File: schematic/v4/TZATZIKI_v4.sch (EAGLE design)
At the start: 7 parts, among them J1 2X20-CHIP-HEADERS2X20CHIP_OFF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

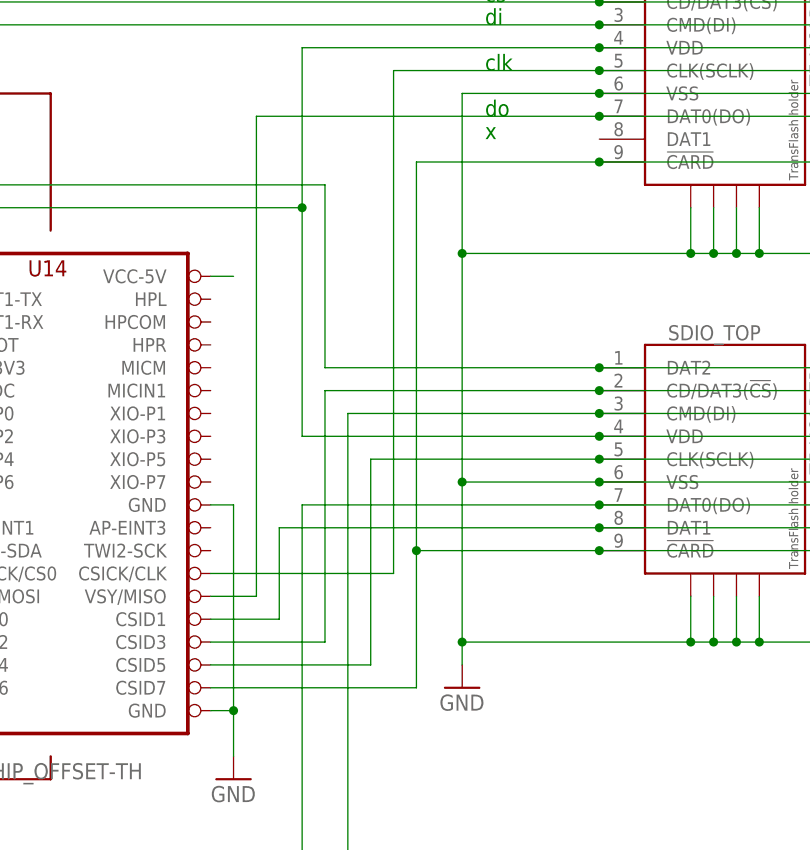
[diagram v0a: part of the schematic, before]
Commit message: moved to eint3 for Card detection
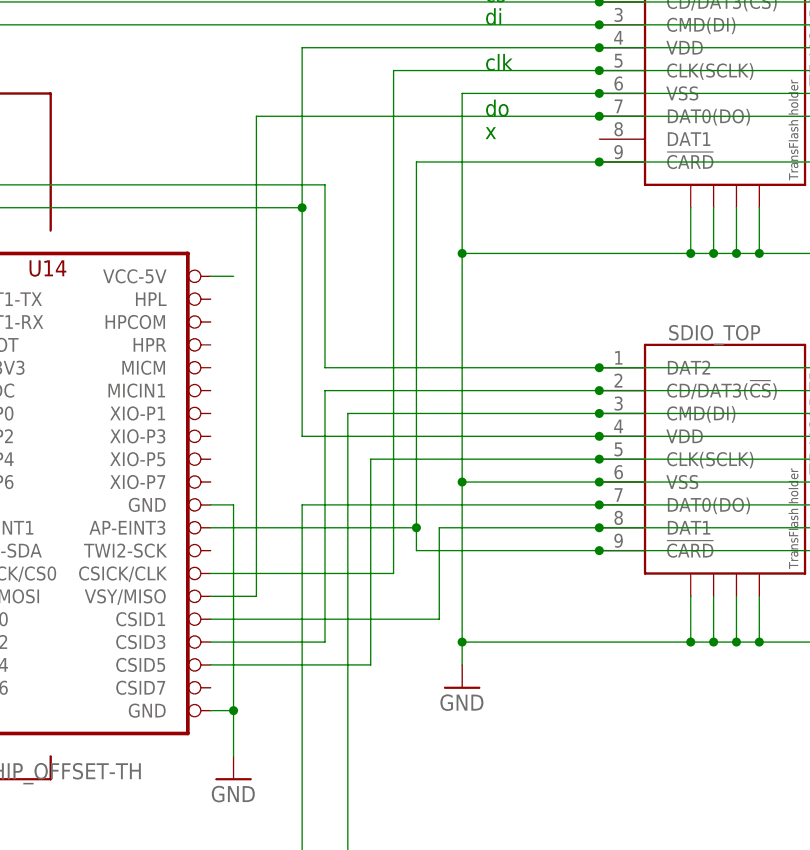
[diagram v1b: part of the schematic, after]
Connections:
- net N$16: now also J1.AP-EINT3; no longer J1.CSID7
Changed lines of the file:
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@@
 <segment>
 <pinref part="J1" gate="G$1" pin="CSID1"/>
-<wire x1="109.22" y1="25.4" x2="116.84" y2="25.4" width="0.1524" layer="91"/>
-<wire x1="116.84" y1="25.4" x2="116.84" y2="35.56" width="0.1524" layer="91"/>
+<wire x1="109.22" y1="25.4" x2="134.62" y2="25.4" width="0.1524" layer="91"/>
+<wire x1="134.62" y1="25.4" x2="134.62" y2="35.56" width="0.1524" layer="91"/>
 <wire x1="185.42" y1="35.56" x2="152.4" y2="35.56" width="0.1524" layer="91"/>
 <pinref part="SDIO_BOT" gate="G$1" pin="DAT1"/>
 <pinref part="SDIO_TOP" gate="G$1" pin="DAT1"/>
-<wire x1="152.4" y1="35.56" x2="116.84" y2="35.56" width="0.1524" layer="91"/>
+<wire x1="152.4" y1="35.56" x2="134.62" y2="35.56" width="0.1524" layer="91"/>
 <junction x="152.4" y="35.56"/>
 </segment>
@@
 <wire x1="185.42" y1="76.2" x2="152.4" y2="76.2" width="0.1524" layer="91"/>
 <pinref part="SDIO_TOP" gate="G$1" pin="!CARD"/>
-<pinref part="J1" gate="G$1" pin="CSID7"/>
-<wire x1="109.22" y1="17.78" x2="132.08" y2="17.78" width="0.1524" layer="91"/>
-<wire x1="132.08" y1="17.78" x2="132.08" y2="33.02" width="0.1524" layer="91"/>
 <wire x1="132.08" y1="33.02" x2="152.4" y2="33.02" width="0.1524" layer="91"/>
 <pinref part="SDIO_BOT" gate="G$1" pin="!CARD"/>
@@
 <junction x="152.4" y="33.02"/>
 <wire x1="152.4" y1="76.2" x2="132.08" y2="76.2" width="0.1524" layer="91"/>
-<wire x1="132.08" y1="76.2" x2="132.08" y2="33.02" width="0.1524" layer="91"/>
-<junction x="132.08" y="33.02"/>
+<wire x1="132.08" y1="76.2" x2="132.08" y2="35.56" width="0.1524" layer="91"/>
 <junction x="152.4" y="76.2"/>
+<pinref part="J1" gate="G$1" pin="AP-EINT3"/>
+<wire x1="132.08" y1="35.56" x2="132.08" y2="33.02" width="0.1524" layer="91"/>
+<wire x1="109.22" y1="35.56" x2="132.08" y2="35.56" width="0.1524" layer="91"/>
+<junction x="132.08" y="35.56"/>
 </segment>
 </net>

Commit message: added gerber
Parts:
- removed SPI_BOT, SPI_TOP: TF-HOLDER, JKW_CHIP:TF-HOLDER
- added R10: 2.2k, rcl:R-EU_R0805
- added U2: DS2431P, JKW_CHIP:DS2431P
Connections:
- removed net N$11: J1.CSIPCK/CS0, SPI_BOT.CD/DAT3(!CS!), SPI_TOP.CD/DAT3(!CS!)
- removed net N$12: J1.HSY/MOSI, SPI_BOT.CMD(DI), SPI_TOP.CMD(DI)
- removed net N$13: J1.VSY/MISO, SPI_BOT.DAT0(DO), SPI_TOP.DAT0(DO)
- removed net N$14: J1.CSICK/CLK, SPI_BOT.CLK(SCLK), SPI_TOP.CLK(SCLK)
- new net LD2: J1.LCD-D2, R10.1, U2.IO
- new net N$1: J1.VCC3V3@2, R10.2
- net GND: now also U2.GND; no longer SPI_BOT.S1, SPI_BOT.S2, SPI_BOT.S3, SPI_BOT.S4, SPI_BOT.VSS, SPI_TOP.S1, SPI_TOP.S2, SPI_TOP.S3, SPI_TOP.S4, SPI_TOP.VSS
- net N$10: no longer SPI_BOT.VDD, SPI_TOP.VDD
- net N$16: no longer SPI_BOT.!CARD, SPI_TOP.!CARD
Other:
- note removed: "clk"
- note removed: "cs"
- note removed: "di"
- note removed: "do"
- note removed: "x"
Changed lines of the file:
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@@
 <part name="SDIO_BOT" library="JKW_CHIP" deviceset="TF-HOLDER" device=""/>
 <part name="SDIO_TOP" library="JKW_CHIP" deviceset="TF-HOLDER" device=""/>
-<part name="SPI_TOP" library="JKW_CHIP" deviceset="TF-HOLDER" device=""/>
-<part name="SPI_BOT" library="JKW_CHIP" deviceset="TF-HOLDER" device=""/>
+<part name="GND14" library="supply1" deviceset="GND" device=""/>
+<part name="R10" library="rcl" deviceset="R-EU_" device="R0805" value="2.2k"/>
+<part name="U2" library="JKW_CHIP" deviceset="DS2431" device="P"/>
 </parts>
 <sheets>
 <sheet>
 <plain>
-<text x="139.7" y="93.98" size="1.778" layer="91">cs</text>
-<text x="139.7" y="91.44" size="1.778" layer="91">di</text>
-<text x="139.7" y="86.36" size="1.778" layer="91">clk</text>
-<text x="139.7" y="81.28" size="1.778" layer="91">do</text>
-<text x="139.7" y="78.74" size="1.778" layer="91">x</text>
-<text x="139.7" y="96.52" size="1.778" layer="91">x</text>
 </plain>
 <instances>
@@
 <instance part="SDIO_BOT" gate="G$1" x="198.12" y="43.18"/>
 <instance part="SDIO_TOP" gate="G$1" x="165.1" y="43.18"/>
-<instance part="SPI_TOP" gate="G$1" x="165.1" y="86.36"/>
-<instance part="SPI_BOT" gate="G$1" x="198.12" y="86.36"/>
+<instance part="GND14" gate="1" x="-35.56" y="12.7" rot="MR0"/>
+<instance part="R10" gate="G$1" x="-7.62" y="43.18" rot="MR90"/>
+<instance part="U2" gate="G$1" x="-33.02" y="33.02"/>
 </instances>
 <busses>
@@
 <wire x1="137.16" y1="40.64" x2="137.16" y2="22.86" width="0.1524" layer="91"/>
 <junction x="137.16" y="22.86"/>
-<wire x1="137.16" y1="83.82" x2="137.16" y2="66.04" width="0.1524" layer="91"/>
-<wire x1="137.16" y1="40.64" x2="137.16" y2="66.04" width="0.1524" layer="91"/>
-<junction x="137.16" y="66.04"/>
-<junction x="137.16" y="40.64"/>
 <wire x1="203.2" y1="22.86" x2="200.66" y2="22.86" width="0.1524" layer="91"/>
 <wire x1="200.66" y1="22.86" x2="198.12" y2="22.86" width="0.1524" layer="91"/>
@@
 <wire x1="185.42" y1="40.64" x2="152.4" y2="40.64" width="0.1524" layer="91"/>
 <wire x1="152.4" y1="40.64" x2="137.16" y2="40.64" width="0.1524" layer="91"/>
-<pinref part="SPI_BOT" gate="G$1" pin="VSS"/>
-<wire x1="137.16" y1="83.82" x2="152.4" y2="83.82" width="0.1524" layer="91"/>
-<pinref part="SPI_TOP" gate="G$1" pin="S1"/>
-<wire x1="152.4" y1="83.82" x2="185.42" y2="83.82" width="0.1524" layer="91"/>
-<wire x1="137.16" y1="66.04" x2="162.56" y2="66.04" width="0.1524" layer="91"/>
-<wire x1="162.56" y1="66.04" x2="162.56" y2="71.12" width="0.1524" layer="91"/>
-<pinref part="SPI_BOT" gate="G$1" pin="S4"/>
-<wire x1="162.56" y1="66.04" x2="165.1" y2="66.04" width="0.1524" layer="91"/>
-<wire x1="165.1" y1="66.04" x2="167.64" y2="66.04" width="0.1524" layer="91"/>
-<wire x1="167.64" y1="66.04" x2="170.18" y2="66.04" width="0.1524" layer="91"/>
-<wire x1="170.18" y1="66.04" x2="195.58" y2="66.04" width="0.1524" layer="91"/>
-<wire x1="195.58" y1="66.04" x2="198.12" y2="66.04" width="0.1524" layer="91"/>
-<wire x1="198.12" y1="66.04" x2="200.66" y2="66.04" width="0.1524" layer="91"/>
-<wire x1="200.66" y1="66.04" x2="203.2" y2="66.04" width="0.1524" layer="91"/>
-<wire x1="203.2" y1="66.04" x2="203.2" y2="71.12" width="0.1524" layer="91"/>
-<pinref part="SPI_BOT" gate="G$1" pin="S3"/>
-<wire x1="200.66" y1="71.12" x2="200.66" y2="66.04" width="0.1524" layer="91"/>
-<pinref part="SPI_BOT" gate="G$1" pin="S2"/>
-<wire x1="198.12" y1="71.12" x2="198.12" y2="66.04" width="0.1524" layer="91"/>
-<pinref part="SPI_BOT" gate="G$1" pin="S1"/>
-<wire x1="195.58" y1="71.12" x2="195.58" y2="66.04" width="0.1524" layer="91"/>
-<pinref part="SPI_TOP" gate="G$1" pin="S4"/>
-<wire x1="170.18" y1="71.12" x2="170.18" y2="66.04" width="0.1524" layer="91"/>
-<pinref part="SPI_TOP" gate="G$1" pin="S3"/>
-<wire x1="167.64" y1="71.12" x2="167.64" y2="66.04" width="0.1524" layer="91"/>
-<pinref part="SPI_TOP" gate="G$1" pin="S2"/>
-<wire x1="165.1" y1="71.12" x2="165.1" y2="66.04" width="0.1524" layer="91"/>
-<junction x="162.56" y="66.04"/>
-<junction x="165.1" y="66.04"/>
-<junction x="167.64" y="66.04"/>
-<junction x="170.18" y="66.04"/>
-<junction x="195.58" y="66.04"/>
-<junction x="198.12" y="66.04"/>
-<junction x="200.66" y="66.04"/>
-<pinref part="SPI_TOP" gate="G$1" pin="VSS"/>
-<junction x="152.4" y="83.82"/>
 <pinref part="SDIO_BOT" gate="G$1" pin="VSS"/>
 <pinref part="SDIO_TOP" gate="G$1" pin="VSS"/>
@@
 <wire x1="-12.7" y1="76.2" x2="-12.7" y2="73.66" width="0.1524" layer="91"/>
 </segment>
+<segment>
+<pinref part="GND14" gate="1" pin="GND"/>
+<wire x1="-35.56" y1="20.32" x2="-35.56" y2="15.24" width="0.1524" layer="91"/>
+<pinref part="U2" gate="G$1" pin="GND"/>
+</segment>
 </net>
 <net name="N$2" class="0">
@@
 <wire x1="71.12" y1="71.12" x2="119.38" y2="71.12" width="0.1524" layer="91"/>
 <wire x1="119.38" y1="71.12" x2="119.38" y2="45.72" width="0.1524" layer="91"/>
-<wire x1="119.38" y1="71.12" x2="119.38" y2="88.9" width="0.1524" layer="91"/>
-<junction x="119.38" y="71.12"/>
 <wire x1="185.42" y1="45.72" x2="152.4" y2="45.72" width="0.1524" layer="91"/>
-<pinref part="SPI_BOT" gate="G$1" pin="VDD"/>
 <wire x1="152.4" y1="45.72" x2="119.38" y2="45.72" width="0.1524" layer="91"/>
-<wire x1="119.38" y1="88.9" x2="152.4" y2="88.9" width="0.1524" layer="91"/>
-<pinref part="SPI_TOP" gate="G$1" pin="VDD"/>
-<wire x1="152.4" y1="88.9" x2="185.42" y2="88.9" width="0.1524" layer="91"/>
-<junction x="152.4" y="88.9"/>
 <pinref part="SDIO_BOT" gate="G$1" pin="VDD"/>
 <pinref part="SDIO_TOP" gate="G$1" pin="VDD"/>
@@
 </segment>
 </net>
-<net name="N$11" class="0">
-<segment>
-<wire x1="152.4" y1="93.98" x2="66.04" y2="93.98" width="0.1524" layer="91"/>
-<wire x1="66.04" y1="93.98" x2="66.04" y2="30.48" width="0.1524" layer="91"/>
-<pinref part="J1" gate="G$1" pin="CSIPCK/CS0"/>
-<wire x1="66.04" y1="30.48" x2="76.2" y2="30.48" width="0.1524" layer="91"/>
-<pinref part="SPI_TOP" gate="G$1" pin="CD/DAT3(!CS!)"/>
-<pinref part="SPI_BOT" gate="G$1" pin="CD/DAT3(!CS!)"/>
-<wire x1="152.4" y1="93.98" x2="185.42" y2="93.98" width="0.1524" layer="91"/>
-<junction x="152.4" y="93.98"/>
-</segment>
-</net>
-<net name="N$12" class="0">
-<segment>
-<wire x1="63.5" y1="91.44" x2="63.5" y2="27.94" width="0.1524" layer="91"/>
-<pinref part="J1" gate="G$1" pin="HSY/MOSI"/>
-<wire x1="63.5" y1="27.94" x2="76.2" y2="27.94" width="0.1524" layer="91"/>
-<pinref part="SPI_BOT" gate="G$1" pin="CMD(DI)"/>
-<wire x1="63.5" y1="91.44" x2="152.4" y2="91.44" width="0.1524" layer="91"/>
-<pinref part="SPI_TOP" gate="G$1" pin="CMD(DI)"/>
-<wire x1="152.4" y1="91.44" x2="185.42" y2="91.44" width="0.1524" layer="91"/>
-<junction x="152.4" y="91.44"/>
-</segment>
-</net>
-<net name="N$13" class="0">
-<segment>
-<pinref part="J1" gate="G$1" pin="VSY/MISO"/>
-<wire x1="109.22" y1="27.94" x2="114.3" y2="27.94" width="0.1524" layer="91"/>
-<wire x1="114.3" y1="27.94" x2="114.3" y2="81.28" width="0.1524" layer="91"/>
-<pinref part="SPI_BOT" gate="G$1" pin="DAT0(DO)"/>
-<wire x1="114.3" y1="81.28" x2="152.4" y2="81.28" width="0.1524" layer="91"/>
-<pinref part="SPI_TOP" gate="G$1" pin="DAT0(DO)"/>
-<wire x1="152.4" y1="81.28" x2="185.42" y2="81.28" width="0.1524" layer="91"/>
-<junction x="152.4" y="81.28"/>
-</segment>
-</net>
 <net name="N$7" class="0">
 <segment>
 <pinref part="J1" gate="G$1" pin="VCC-5V@2"/>
 <wire x1="109.22" y1="63.5" x2="111.76" y2="63.5" width="0.1524" layer="91"/>
-</segment>
-</net>
-<net name="N$14" class="0">
-<segment>
-<wire x1="129.54" y1="30.48" x2="129.54" y2="86.36" width="0.1524" layer="91"/>
-<pinref part="J1" gate="G$1" pin="CSICK/CLK"/>
-<wire x1="109.22" y1="30.48" x2="129.54" y2="30.48" width="0.1524" layer="91"/>
-<pinref part="SPI_BOT" gate="G$1" pin="CLK(SCLK)"/>
-<wire x1="129.54" y1="86.36" x2="152.4" y2="86.36" width="0.1524" layer="91"/>
-<pinref part="SPI_TOP" gate="G$1" pin="CLK(SCLK)"/>
-<wire x1="152.4" y1="86.36" x2="185.42" y2="86.36" width="0.1524" layer="91"/>
-<junction x="152.4" y="86.36"/>
 </segment>
 </net>
@@
 <net name="N$16" class="0">
 <segment>
-<pinref part="SPI_BOT" gate="G$1" pin="!CARD"/>
-<pinref part="SPI_TOP" gate="G$1" pin="!CARD"/>
-<wire x1="185.42" y1="76.2" x2="152.4" y2="76.2" width="0.1524" layer="91"/>
 <pinref part="SDIO_TOP" gate="G$1" pin="!CARD"/>
 <wire x1="132.08" y1="33.02" x2="152.4" y2="33.02" width="0.1524" layer="91"/>
@@
 <wire x1="185.42" y1="33.02" x2="152.4" y2="33.02" width="0.1524" layer="91"/>
 <junction x="152.4" y="33.02"/>
-<wire x1="152.4" y1="76.2" x2="132.08" y2="76.2" width="0.1524" layer="91"/>
-<wire x1="132.08" y1="76.2" x2="132.08" y2="35.56" width="0.1524" layer="91"/>
-<junction x="152.4" y="76.2"/>
 <pinref part="J1" gate="G$1" pin="AP-EINT3"/>
 <wire x1="132.08" y1="35.56" x2="132.08" y2="33.02" width="0.1524" layer="91"/>
 <wire x1="109.22" y1="35.56" x2="132.08" y2="35.56" width="0.1524" layer="91"/>
-<junction x="132.08" y="35.56"/>
-</segment>
-</net>
+</segment>
+</net>
+<net name="LD2" class="0">
+<segment>
+<label x="-12.7" y="35.56" size="1.778" layer="95" rot="MR0"/>
+<wire x1="-22.86" y1="35.56" x2="-7.62" y2="35.56" width="0.1524" layer="91"/>
+<pinref part="R10" gate="G$1" pin="1"/>
+<wire x1="-7.62" y1="35.56" x2="-2.54" y2="35.56" width="0.1524" layer="91"/>
+<wire x1="-7.62" y1="38.1" x2="-7.62" y2="35.56" width="0.1524" layer="91"/>
+<junction x="-7.62" y="35.56"/>
+<pinref part="U2" gate="G$1" pin="IO"/>
+<pinref part="J1" gate="G$1" pin="LCD-D2"/>
+<wire x1="12.7" y1="43.18" x2="-2.54" y2="43.18" width="0.1524" layer="91"/>
+<wire x1="-2.54" y1="43.18" x2="-2.54" y2="35.56" width="0.1524" layer="91"/>
+</segment>
+</net>
+<net name="N$1" class="0">
+<segment>
+<pinref part="R10" gate="G$1" pin="2"/>
+<pinref part="J1" gate="G$1" pin="VCC3V3@2"/>
+<wire x1="12.7" y1="58.42" x2="-7.62" y2="58.42" width="0.1524" layer="91"/>
+<wire x1="-7.62" y1="58.42" x2="-7.62" y2="48.26" width="0.1524" layer="91"/>
+</segment>
+</net>
